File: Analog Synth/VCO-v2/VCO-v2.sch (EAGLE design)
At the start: 19 parts, among them IC1 TL084D, U1 CA3096

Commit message: VCO-v2 progress: linear voltage to exponential current converter and hysteresis circuit
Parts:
- added C1: 10n, resistor:C-EU025-025X050
- added C2: 1u, resistor:C-EU025-050X050
- added C3: 100u, resistor:C-EU050-075X075
- added C4: 100p, resistor:C-EU025-025X050
- added C5: 100p, resistor:C-EU025-050X050
- added FREQ-RNGE: (no value), switch:255SB
- added IC2: TL084P, linear:TL084P
- added R10, R16, R18: 10k, resistor:R-US_0204/7
- added R13, R15, R17, R19: 2.2k, resistor:R-US_0204/7
- added R20: 100k, resistor:R-US_0204/7
- added R7: 150k, resistor:R-US_0204/7
- added R8: 1k, resistor:R-US_0204/7
- added R9: 4.7k, resistor:R-US_0204/7
- added T1, T2, T3: 2N3904, transistor-neu-to92:2N3904
- added U$1, U$2: 2N7000, !synth_sch:2N7000
- IC1: value TL084D -> TL084P; device linear:TL084D -> linear:TL084P
- R1, R11, R12, R14, R2, R3, R4, R5, R6: device resistor:R-US_M0805 -> resistor:R-US_0204/7
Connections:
- new net +9V: R16.2, R17.1, R19.2
- new net -12V: U1G$6.E
- new net -9V: R10.1, R9.1
- new net N$12: U1G$2.C, U1G$4.B, U1G$4.C, U1G$5.B
- new net N$14: C4.2, IC2A.OUT, R8.1
- new net N$15: R8.2, U1G$1.E, U1G$2.E, U1G$3.E
- new net N$16: R16.1, T1.C, T2.B
- new net N$18: C2.1, FREQ-RNGE.S
- new net N$19: U$1.S, U1G$3.C
- new net N$20: U$2.D, U1G$5.C
- new net N$21: C4.1, IC2A.-IN, R7.1, U1G$1.C
- new net N$22: C3.1, FREQ-RNGE.O
- new net N$23: R10.2, R13.1, R18.1, R9.2, T1.B
- new net N$24: R13.2, R15.1
- new net N$30: C5.2, R20.1, T3.B
- new net RAMP_DOWN: C5.1, R17.2, R18.2, R20.2, T2.C, U$1.G
- new net RAMP_UP: R19.1, T3.C, U$2.G
- new net TRIANGLE-RAW: C1.1, FREQ-RNGE.P, IC2B.+IN, U$1.D, U$2.S
- new net V-CAP-BUFF: IC2B.-IN, IC2B.OUT, R15.2
- net +5V: now also R7.2, U1G$4.E, U1G$5.E
- net -5V: now also C1.2, C2.2, C3.2, T1.E, T2.E, T3.E, U1G$2.B, U1G$3.B
- net GND: now also IC2A.+IN
- net NPN_CV: now also U1G$1.B
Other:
- note added: "All of the devices inside the dashed box belong to the CA3096 transistor array chip. Note: None of the devices are internally connected; connections between the array's transistors must be made externally."
- note added: "CA3096"
- note added: "ON-OFF-ON"

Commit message: VCO-v2 high frequency compensation
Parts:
- added C6, C7: 300p, resistor:C-EU025-050X050
- added HIGH-FREQ: 100k trim, pot:TRIM_US-B64Y
- added Q1, Q2: J310, transistor-small-signal:J310
- added R21, R23, R24, R26: 10k, resistor:R-US_0204/7
- added R22, R25: 100k, resistor:R-US_0204/7
- added R27: 47k, resistor:R-US_0204/7
- added T4, T7: 2N3904, transistor-neu-to92:2N3904
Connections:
- new net N$25: Q1.D, R21.1, R23.1
- new net N$26: C7.2, Q1.G, R22.2, T7.B
- new net N$29: Q2.D, R24.1, R26.1
- new net N$31: C6.2, Q2.G, R25.2, T4.B
- new net N$32: HIGH-FREQ.A, R23.2, R26.2
- new net N$33: HIGH-FREQ.S, R27.1
- net -5V: now also HIGH-FREQ.E, Q1.S, Q2.S, R22.1, R25.1
- net CV_SUM_POINT: now also R27.2
- net GND: now also R21.2, R24.2, T4.C, T4.E, T7.C, T7.E
- net RAMP_DOWN: now also C6.1
- net RAMP_UP: now also C7.1

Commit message: VCO-v2
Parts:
- added U$3: EURORACK-POWER, !synth_sch:EURORACK-POWER
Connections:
- new net N$27: U$3.P$3, U$3.P$5, U$3.P$7
- new net N$28: U$3.P$4, U$3.P$6, U$3.P$8
- new net N$34: U$3.P$1, U$3.P$2
- new net N$35: U$3.P$10, U$3.P$9
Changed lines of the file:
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@@
 <part name="R27" library="resistor" deviceset="R-US_" device="0204/7" value="47k"/>
 <part name="SUPPLY27" library="supply2" deviceset="-5V" device=""/>
+<part name="U$3" library="!synth_sch" deviceset="EURORACK-POWER" device=""/>
 </parts>
 <sheets>
@@
 </instance>
 <instance part="IC2" gate="B" x="152.4" y="66.04" rot="MR180"/>
-<instance part="IC2" gate="C" x="200.66" y="55.88"/>
-<instance part="IC2" gate="D" x="226.06" y="50.8"/>
 <instance part="R8" gate="G$1" x="33.02" y="20.32"/>
 <instance part="C4" gate="G$1" x="10.16" y="30.48" rot="R90"/>
@@
 </segment>
 </net>
+</nets>
+</sheet>
+<sheet>
+<plain>
+</plain>
+<instances>
+<instance part="IC2" gate="C" x="7.62" y="35.56"/>
+<instance part="IC2" gate="D" x="38.1" y="35.56"/>
+</instances>
+<busses>
+</busses>
+<nets>
+</nets>
+</sheet>
+<sheet>
+<description>Power
+This part of the circuit handles the input +-12 V supply lines. It creates internal regulated voltage supplies for +5, +9, -5, and -9 V.</description>
+<plain>
+</plain>
+<instances>
+<instance part="U$3" gate="G$1" x="2.54" y="50.8"/>
+</instances>
+<busses>
+</busses>
+<nets>
+<net name="N$27" class="0">
+<segment>
+<pinref part="U$3" gate="G$1" pin="P$3"/>
+<wire x1="0" y1="55.88" x2="-5.08" y2="55.88" width="0.1524" layer="91"/>
+<wire x1="-5.08" y1="55.88" x2="-5.08" y2="50.8" width="0.1524" layer="91"/>
+<pinref part="U$3" gate="G$1" pin="P$5"/>
+<wire x1="0" y1="50.8" x2="-5.08" y2="50.8" width="0.1524" layer="91"/>
+<wire x1="-5.08" y1="50.8" x2="-5.08" y2="45.72" width="0.1524" layer="91"/>
+<pinref part="U$3" gate="G$1" pin="P$7"/>
+<wire x1="-5.08" y1="45.72" x2="0" y2="45.72" width="0.1524" layer="91"/>
+<junction x="-5.08" y="50.8"/>
+</segment>
+</net>
+<net name="N$28" class="0">
+<segment>
+<pinref part="U$3" gate="G$1" pin="P$8"/>
+<wire x1="2.54" y1="45.72" x2="7.62" y2="45.72" width="0.1524" layer="91"/>
+<wire x1="7.62" y1="45.72" x2="7.62" y2="50.8" width="0.1524" layer="91"/>
+<pinref part="U$3" gate="G$1" pin="P$6"/>
+<wire x1="2.54" y1="50.8" x2="7.62" y2="50.8" width="0.1524" layer="91"/>
+<wire x1="7.62" y1="50.8" x2="7.62" y2="55.88" width="0.1524" layer="91"/>
+<pinref part="U$3" gate="G$1" pin="P$4"/>
+<wire x1="7.62" y1="55.88" x2="2.54" y2="55.88" width="0.1524" layer="91"/>
+<junction x="7.62" y="50.8"/>
+</segment>
+</net>
+<net name="N$34" class="0">
+<segment>
+<pinref part="U$3" gate="G$1" pin="P$1"/>
+<wire x1="0" y1="60.96" x2="-5.08" y2="60.96" width="0.1524" layer="91"/>
+<wire x1="-5.08" y1="60.96" x2="-5.08" y2="66.04" width="0.1524" layer="91"/>
+<wire x1="-5.08" y1="66.04" x2="2.54" y2="66.04" width="0.1524" layer="91"/>
+<wire x1="2.54" y1="66.04" x2="7.62" y2="66.04" width="0.1524" layer="91"/>
+<wire x1="7.62" y1="66.04" x2="7.62" y2="60.96" width="0.1524" layer="91"/>
+<pinref part="U$3" gate="G$1" pin="P$2"/>
+<wire x1="7.62" y1="60.96" x2="2.54" y2="60.96" width="0.1524" layer="91"/>
+<wire x1="2.54" y1="66.04" x2="2.54" y2="68.58" width="0.1524" layer="91"/>
+<junction x="2.54" y="66.04"/>
+</segment>
+</net>
+<net name="N$35" class="0">
+<segment>
+<pinref part="U$3" gate="G$1" pin="P$9"/>
+<wire x1="0" y1="40.64" x2="-5.08" y2="40.64" width="0.1524" layer="91"/>
+<wire x1="-5.08" y1="40.64" x2="-5.08" y2="35.56" width="0.1524" layer="91"/>
+<wire x1="-5.08" y1="35.56" x2="2.54" y2="35.56" width="0.1524" layer="91"/>
+<wire x1="2.54" y1="35.56" x2="7.62" y2="35.56" width="0.1524" layer="91"/>
+<wire x1="7.62" y1="35.56" x2="7.62" y2="40.64" width="0.1524" layer="91"/>
+<pinref part="U$3" gate="G$1" pin="P$10"/>
+<wire x1="7.62" y1="40.64" x2="2.54" y2="40.64" width="0.1524" layer="91"/>
+<wire x1="2.54" y1="35.56" x2="2.54" y2="33.02" width="0.1524" layer="91"/>
+<junction x="2.54" y="35.56"/>
+</segment>
+</net>

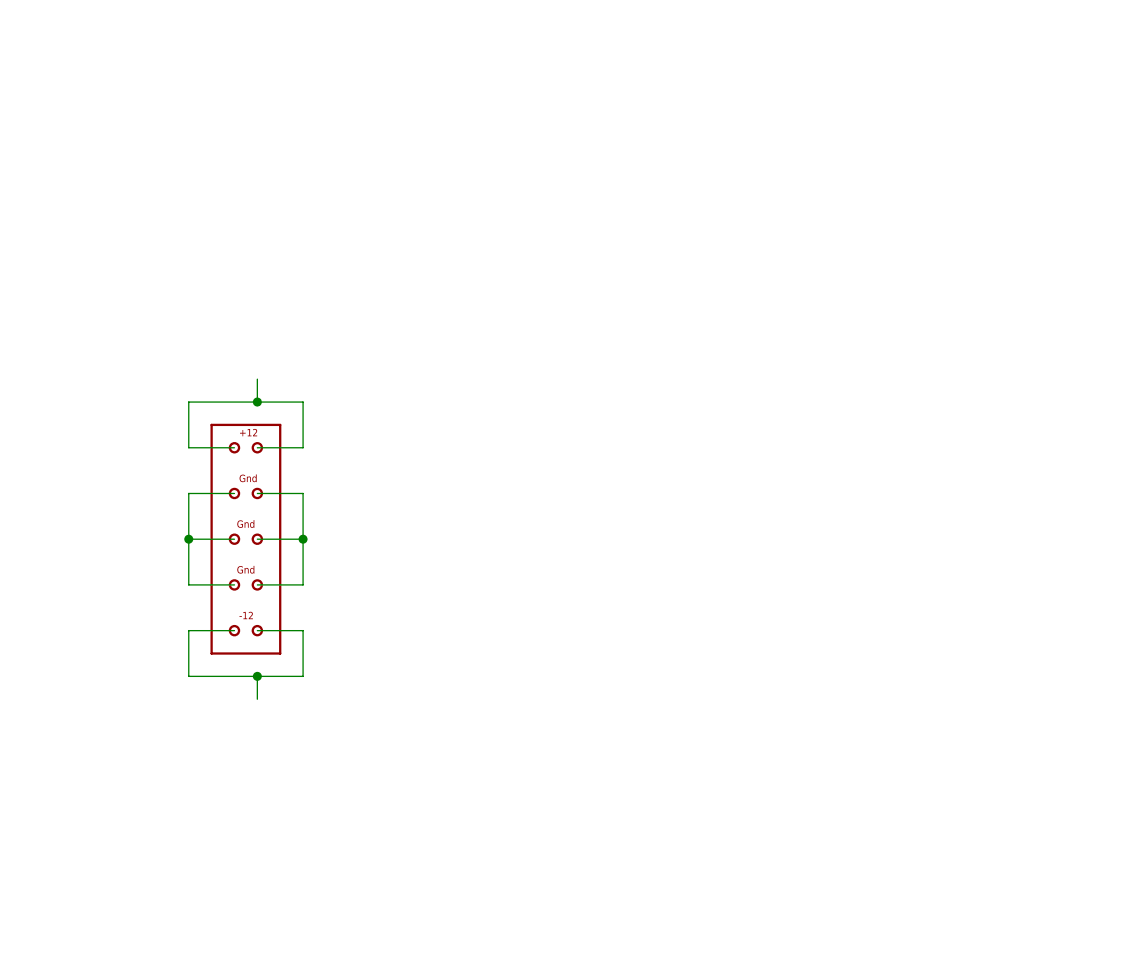
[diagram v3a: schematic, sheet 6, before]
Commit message: VCO-v2 - power supply. Also, I need to change those integration caps to be polarized types in the schematic and on the pcb...
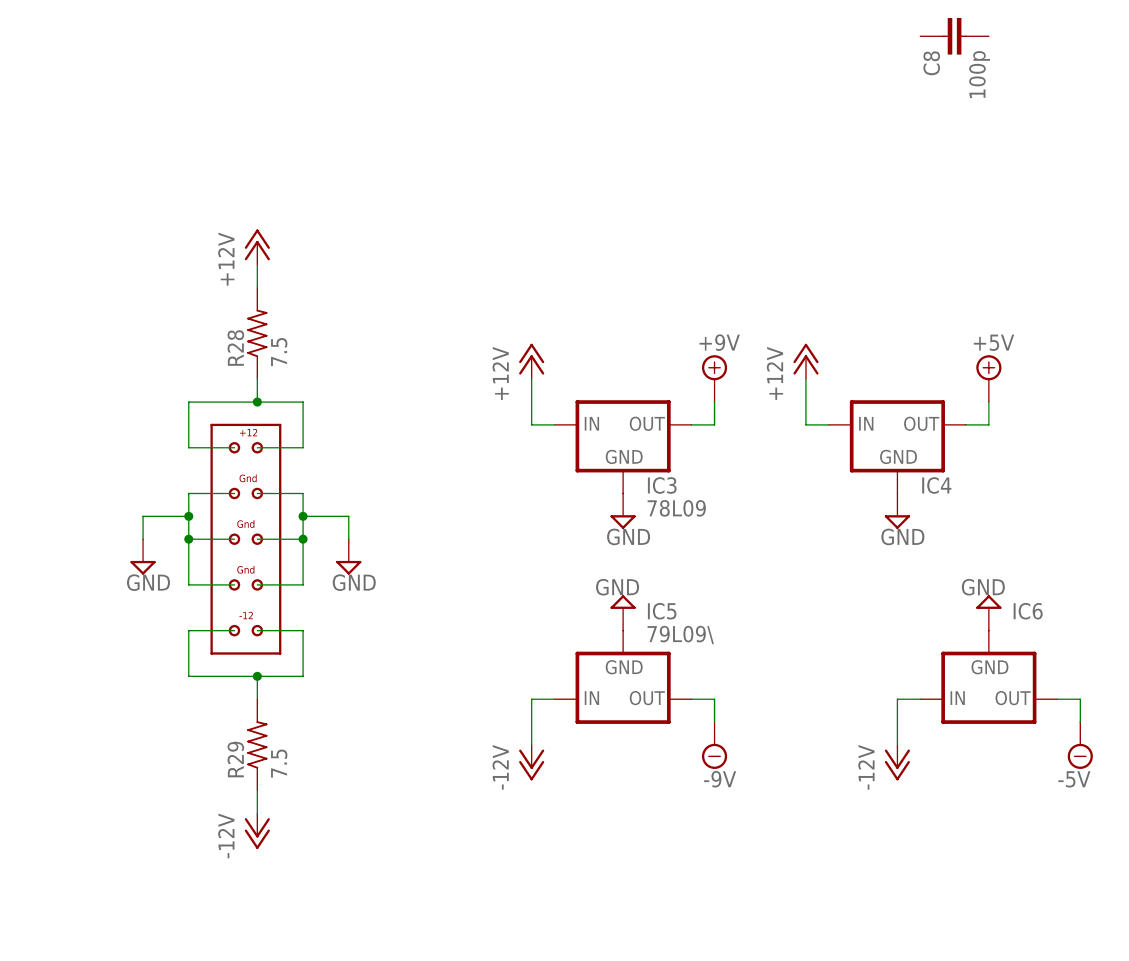
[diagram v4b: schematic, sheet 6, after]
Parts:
- added C8: 100p, resistor:C-EU025-050X050
- added IC3: 78L09, v-reg:78LXX
- added IC4: (no value), v-reg:78LXX
- added IC5: 79L09\, v-reg:79LXX
- added IC6: (no value), v-reg:79LXX
- added R28, R29: 7.5, resistor:R-US_0204/7
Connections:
- removed net N$27: U$3.P$3, U$3.P$5, U$3.P$7
- removed net N$28: U$3.P$4, U$3.P$6, U$3.P$8
- new net +12V: IC3.IN, IC4.IN, R28.2
- net +5V: now also IC4.OUT
- net +9V: now also IC3.OUT
- net -12V: now also IC5.IN, IC6.IN, R29.1
- net -5V: now also IC6.OUT
- net -9V: now also IC5.OUT
- net GND: now also IC3.GND, IC4.GND, IC6.GND, U$3.P$3, U$3.P$4, U$3.P$5, U$3.P$6, U$3.P$7, U$3.P$8
- net N$34: now also R28.1
- net N$35: now also R29.2
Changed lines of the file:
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@@
 <part name="SUPPLY27" library="supply2" deviceset="-5V" device=""/>
 <part name="U$3" library="!synth_sch" deviceset="EURORACK-POWER" device=""/>
+<part name="IC3" library="v-reg" deviceset="78LXX" device="" value="78L09"/>
+<part name="IC4" library="v-reg" deviceset="78LXX" device=""/>
+<part name="IC5" library="v-reg" deviceset="79LXX" device="" value="79L09\"/>
+<part name="IC6" library="v-reg" deviceset="79LXX" device=""/>
+<part name="C8" library="resistor" deviceset="C-EU" device="025-050X050" value="100p"/>
+<part name="SUPPLY31" library="supply2" deviceset="-5V" device=""/>
+<part name="R28" library="resistor" deviceset="R-US_" device="0204/7" value="7.5"/>
+<part name="R29" library="resistor" deviceset="R-US_" device="0204/7" value="7.5"/>
+<part name="P-3" library="supply1" deviceset="-12V" device=""/>
+<part name="P+1" library="supply1" deviceset="+12V" device=""/>
+<part name="P+2" library="supply1" deviceset="+12V" device=""/>
+<part name="SUPPLY30" library="supply2" deviceset="+5V" device=""/>
+<part name="SUPPLY32" library="supply2" deviceset="+9V" device=""/>
+<part name="P-4" library="supply1" deviceset="-12V" device=""/>
+<part name="SUPPLY34" library="supply2" deviceset="GND" device=""/>
+<part name="SUPPLY35" library="supply2" deviceset="GND" device=""/>
+<part name="SUPPLY36" library="supply2" deviceset="GND" device=""/>
+<part name="SUPPLY37" library="supply2" deviceset="GND" device=""/>
+<part name="SUPPLY38" library="supply2" deviceset="-9V" device=""/>
+<part name="P+3" library="supply1" deviceset="+12V" device=""/>
+<part name="SUPPLY39" library="supply2" deviceset="GND" device=""/>
+<part name="SUPPLY40" library="supply2" deviceset="GND" device=""/>
+<part name="P-5" library="supply1" deviceset="-12V" device=""/>
 </parts>
 <sheets>
@@
 <instances>
 <instance part="U$3" gate="G$1" x="2.54" y="50.8"/>
+<instance part="IC3" gate="1" x="43.18" y="63.5"/>
+<instance part="IC4" gate="1" x="73.66" y="63.5"/>
+<instance part="IC5" gate="A" x="43.18" y="33.02"/>
+<instance part="IC6" gate="A" x="83.82" y="33.02"/>
+<instance part="C8" gate="G$1" x="78.74" y="106.68" rot="MR270"/>
+<instance part="SUPPLY31" gate="-5V" x="93.98" y="27.94"/>
+<instance part="R28" gate="G$1" x="2.54" y="73.66" rot="R90"/>
+<instance part="R29" gate="G$1" x="2.54" y="27.94" rot="R90"/>
+<instance part="P-3" gate="1" x="2.54" y="17.78"/>
+<instance part="P+1" gate="1" x="2.54" y="83.82"/>
+<instance part="P+2" gate="1" x="33.02" y="71.12"/>
+<instance part="SUPPLY30" gate="+5V" x="83.82" y="68.58"/>
+<instance part="SUPPLY32" gate="G$1" x="53.34" y="68.58"/>
+<instance part="P-4" gate="1" x="33.02" y="25.4"/>
+<instance part="SUPPLY34" gate="GND" x="43.18" y="43.18" rot="R180"/>
+<instance part="SUPPLY35" gate="GND" x="43.18" y="53.34"/>
+<instance part="SUPPLY36" gate="GND" x="12.7" y="48.26"/>
+<instance part="SUPPLY37" gate="GND" x="-10.16" y="48.26"/>
+<instance part="SUPPLY38" gate="G$1" x="53.34" y="27.94"/>
+<instance part="P+3" gate="1" x="63.5" y="71.12"/>
+<instance part="SUPPLY39" gate="GND" x="83.82" y="43.18" rot="R180"/>
+<instance part="SUPPLY40" gate="GND" x="73.66" y="53.34"/>
+<instance part="P-5" gate="1" x="73.66" y="25.4"/>
 </instances>
 <busses>
 </busses>
 <nets>
-<net name="N$27" class="0">
-<segment>
-<pinref part="U$3" gate="G$1" pin="P$3"/>
-<wire x1="0" y1="55.88" x2="-5.08" y2="55.88" width="0.1524" layer="91"/>
-<wire x1="-5.08" y1="55.88" x2="-5.08" y2="50.8" width="0.1524" layer="91"/>
-<pinref part="U$3" gate="G$1" pin="P$5"/>
-<wire x1="0" y1="50.8" x2="-5.08" y2="50.8" width="0.1524" layer="91"/>
-<wire x1="-5.08" y1="50.8" x2="-5.08" y2="45.72" width="0.1524" layer="91"/>
-<pinref part="U$3" gate="G$1" pin="P$7"/>
-<wire x1="-5.08" y1="45.72" x2="0" y2="45.72" width="0.1524" layer="91"/>
-<junction x="-5.08" y="50.8"/>
-</segment>
-</net>
-<net name="N$28" class="0">
-<segment>
-<pinref part="U$3" gate="G$1" pin="P$8"/>
-<wire x1="2.54" y1="45.72" x2="7.62" y2="45.72" width="0.1524" layer="91"/>
-<wire x1="7.62" y1="45.72" x2="7.62" y2="50.8" width="0.1524" layer="91"/>
-<pinref part="U$3" gate="G$1" pin="P$6"/>
-<wire x1="2.54" y1="50.8" x2="7.62" y2="50.8" width="0.1524" layer="91"/>
-<wire x1="7.62" y1="50.8" x2="7.62" y2="55.88" width="0.1524" layer="91"/>
-<pinref part="U$3" gate="G$1" pin="P$4"/>
-<wire x1="7.62" y1="55.88" x2="2.54" y2="55.88" width="0.1524" layer="91"/>
-<junction x="7.62" y="50.8"/>
-</segment>
-</net>
 <net name="N$34" class="0">
 <segment>
@@
 <wire x1="2.54" y1="66.04" x2="2.54" y2="68.58" width="0.1524" layer="91"/>
 <junction x="2.54" y="66.04"/>
+<pinref part="R28" gate="G$1" pin="1"/>
 </segment>
 </net>
@@
 <wire x1="2.54" y1="35.56" x2="2.54" y2="33.02" width="0.1524" layer="91"/>
 <junction x="2.54" y="35.56"/>
-</segment>
-</net>
+<pinref part="R29" gate="G$1" pin="2"/>
+</segment>
+</net>
+<net name="-12V" class="0">
+<segment>
+<pinref part="R29" gate="G$1" pin="1"/>
+<pinref part="P-3" gate="1" pin="-12V"/>
+<wire x1="2.54" y1="20.32" x2="2.54" y2="22.86" width="0.1524" layer="91"/>
+</segment>
+<segment>
+<pinref part="IC5" gate="A" pin="IN"/>
+<wire x1="35.56" y1="33.02" x2="33.02" y2="33.02" width="0.1524" layer="91"/>
+<pinref part="P-4" gate="1" pin="-12V"/>
+<wire x1="33.02" y1="33.02" x2="33.02" y2="27.94" width="0.1524" layer="91"/>
+</segment>
+<segment>
+<pinref part="IC6" gate="A" pin="IN"/>
+<wire x1="76.2" y1="33.02" x2="73.66" y2="33.02" width="0.1524" layer="91"/>
+<wire x1="73.66" y1="33.02" x2="73.66" y2="27.94" width="0.1524" layer="91"/>
+<pinref part="P-5" gate="1" pin="-12V"/>
+</segment>
+</net>
+<net name="+12V" class="0">
+<segment>
+<pinref part="R28" gate="G$1" pin="2"/>
+<pinref part="P+1" gate="1" pin="+12V"/>
+<wire x1="2.54" y1="81.28" x2="2.54" y2="78.74" width="0.1524" layer="91"/>
+</segment>
+<segment>
+<pinref part="IC3" gate="1" pin="IN"/>
+<wire x1="35.56" y1="63.5" x2="33.02" y2="63.5" width="0.1524" layer="91"/>
+<wire x1="33.02" y1="63.5" x2="33.02" y2="68.58" width="0.1524" layer="91"/>
+<pinref part="P+2" gate="1" pin="+12V"/>
+</segment>
+<segment>
+<pinref part="IC4" gate="1" pin="IN"/>
+<wire x1="66.04" y1="63.5" x2="63.5" y2="63.5" width="0.1524" layer="91"/>
+<pinref part="P+3" gate="1" pin="+12V"/>
+<wire x1="63.5" y1="63.5" x2="63.5" y2="68.58" width="0.1524" layer="91"/>
+</segment>
+</net>
+<net name="GND" class="0">
+<segment>
+<pinref part="IC3" gate="1" pin="GND"/>
+<pinref part="SUPPLY35" gate="GND" pin="GND"/>
+</segment>
+<segment>
+<pinref part="SUPPLY36" gate="GND" pin="GND"/>
+<wire x1="12.7" y1="53.34" x2="12.7" y2="50.8" width="0.1524" layer="91"/>
+<pinref part="U$3" gate="G$1" pin="P$8"/>
+<wire x1="2.54" y1="45.72" x2="7.62" y2="45.72" width="0.1524" layer="91"/>
+<wire x1="7.62" y1="45.72" x2="7.62" y2="50.8" width="0.1524" layer="91"/>
+<pinref part="U$3" gate="G$1" pin="P$6"/>
+<wire x1="2.54" y1="50.8" x2="7.62" y2="50.8" width="0.1524" layer="91"/>
+<wire x1="7.62" y1="50.8" x2="7.62" y2="53.34" width="0.1524" layer="91"/>
+<pinref part="U$3" gate="G$1" pin="P$4"/>
+<wire x1="7.62" y1="53.34" x2="7.62" y2="55.88" width="0.1524" layer="91"/>
+<wire x1="7.62" y1="55.88" x2="2.54" y2="55.88" width="0.1524" layer="91"/>
+<junction x="7.62" y="50.8"/>
+<junction x="7.62" y="53.34"/>
+<wire x1="7.62" y1="53.34" x2="12.7" y2="53.34" width="0.1524" layer="91"/>
+</segment>
+<segment>
+<pinref part="SUPPLY37" gate="GND" pin="GND"/>
+<wire x1="-10.16" y1="50.8" x2="-10.16" y2="53.34" width="0.1524" layer="91"/>
+<pinref part="U$3" gate="G$1" pin="P$3"/>
+<wire x1="0" y1="55.88" x2="-5.08" y2="55.88" width="0.1524" layer="91"/>
+<wire x1="-5.08" y1="55.88" x2="-5.08" y2="53.34" width="0.1524" layer="91"/>
+<pinref part="U$3" gate="G$1" pin="P$5"/>
+<wire x1="-5.08" y1="53.34" x2="-5.08" y2="50.8" width="0.1524" layer="91"/>
+<wire x1="0" y1="50.8" x2="-5.08" y2="50.8" width="0.1524" layer="91"/>
+<wire x1="-5.08" y1="50.8" x2="-5.08" y2="45.72" width="0.1524" layer="91"/>
+<pinref part="U$3" gate="G$1" pin="P$7"/>
+<wire x1="-5.08" y1="45.72" x2="0" y2="45.72" width="0.1524" layer="91"/>
+<junction x="-5.08" y="50.8"/>
+<wire x1="-10.16" y1="53.34" x2="-5.08" y2="53.34" width="0.1524" layer="91"/>
+<junction x="-5.08" y="53.34"/>
+</segment>
+<segment>
+<pinref part="IC6" gate="A" pin="GND"/>
+<pinref part="SUPPLY39" gate="GND" pin="GND"/>
+</segment>
+<segment>
+<pinref part="IC4" gate="1" pin="GND"/>
+<pinref part="SUPPLY40" gate="GND" pin="GND"/>
+</segment>
+</net>
+<net name="+9V" class="0">
+<segment>
+<pinref part="IC3" gate="1" pin="OUT"/>
+<wire x1="50.8" y1="63.5" x2="53.34" y2="63.5" width="0.1524" layer="91"/>
+<pinref part="SUPPLY32" gate="G$1" pin="+9V"/>
+<wire x1="53.34" y1="63.5" x2="53.34" y2="66.04" width="0.1524" layer="91"/>
+</segment>
+</net>
+<net name="-9V" class="0">
+<segment>
+<pinref part="IC5" gate="A" pin="OUT"/>
+<wire x1="50.8" y1="33.02" x2="53.34" y2="33.02" width="0.1524" layer="91"/>
+<wire x1="53.34" y1="33.02" x2="53.34" y2="30.48" width="0.1524" layer="91"/>
+<pinref part="SUPPLY38" gate="G$1" pin="-9V"/>
+</segment>
+</net>
+<net name="+5V" class="0">
+<segment>
+<pinref part="IC4" gate="1" pin="OUT"/>
+<wire x1="81.28" y1="63.5" x2="83.82" y2="63.5" width="0.1524" layer="91"/>
+<wire x1="83.82" y1="63.5" x2="83.82" y2="66.04" width="0.1524" layer="91"/>
+<pinref part="SUPPLY30" gate="+5V" pin="+5V"/>
+</segment>
+</net>
+<net name="-5V" class="0">
+<segment>
+<pinref part="IC6" gate="A" pin="OUT"/>
+<wire x1="91.44" y1="33.02" x2="93.98" y2="33.02" width="0.1524" layer="91"/>
+<wire x1="93.98" y1="33.02" x2="93.98" y2="30.48" width="0.1524" layer="91"/>
+<pinref part="SUPPLY31" gate="-5V" pin="-5V"/>
+</segment>
+</net>
